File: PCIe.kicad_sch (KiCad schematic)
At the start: 24 parts, among them J12 10018783-11200TLF, U15 AP64501SP-13

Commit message: removed many unused parts
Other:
- company: © 2020-2022 Raspberry Pi Ltd (formerly Raspberry Pi (Trading) Ltd.) -> (none)
- title: Compute Module 4 IO Board - PCIe -> bitcart - PCIe
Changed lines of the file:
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@@
   (paper "A4")
   (title_block
-    (title "Compute Module 4 IO Board - PCIe")
+    (title "bitcart - PCIe")
+    (date "2022-06-02")
     (rev "1")
-    (company "© 2020-2022 Raspberry Pi Ltd (formerly Raspberry Pi (Trading) Ltd.)")
-    (comment 1 "www.raspberrypi.com")
+    (comment 1 "https://github.com/skot/bitcart.git")
   )
   (junction (at 157.734 152.654) (diameter 1.016) (color 0 0 0 0)

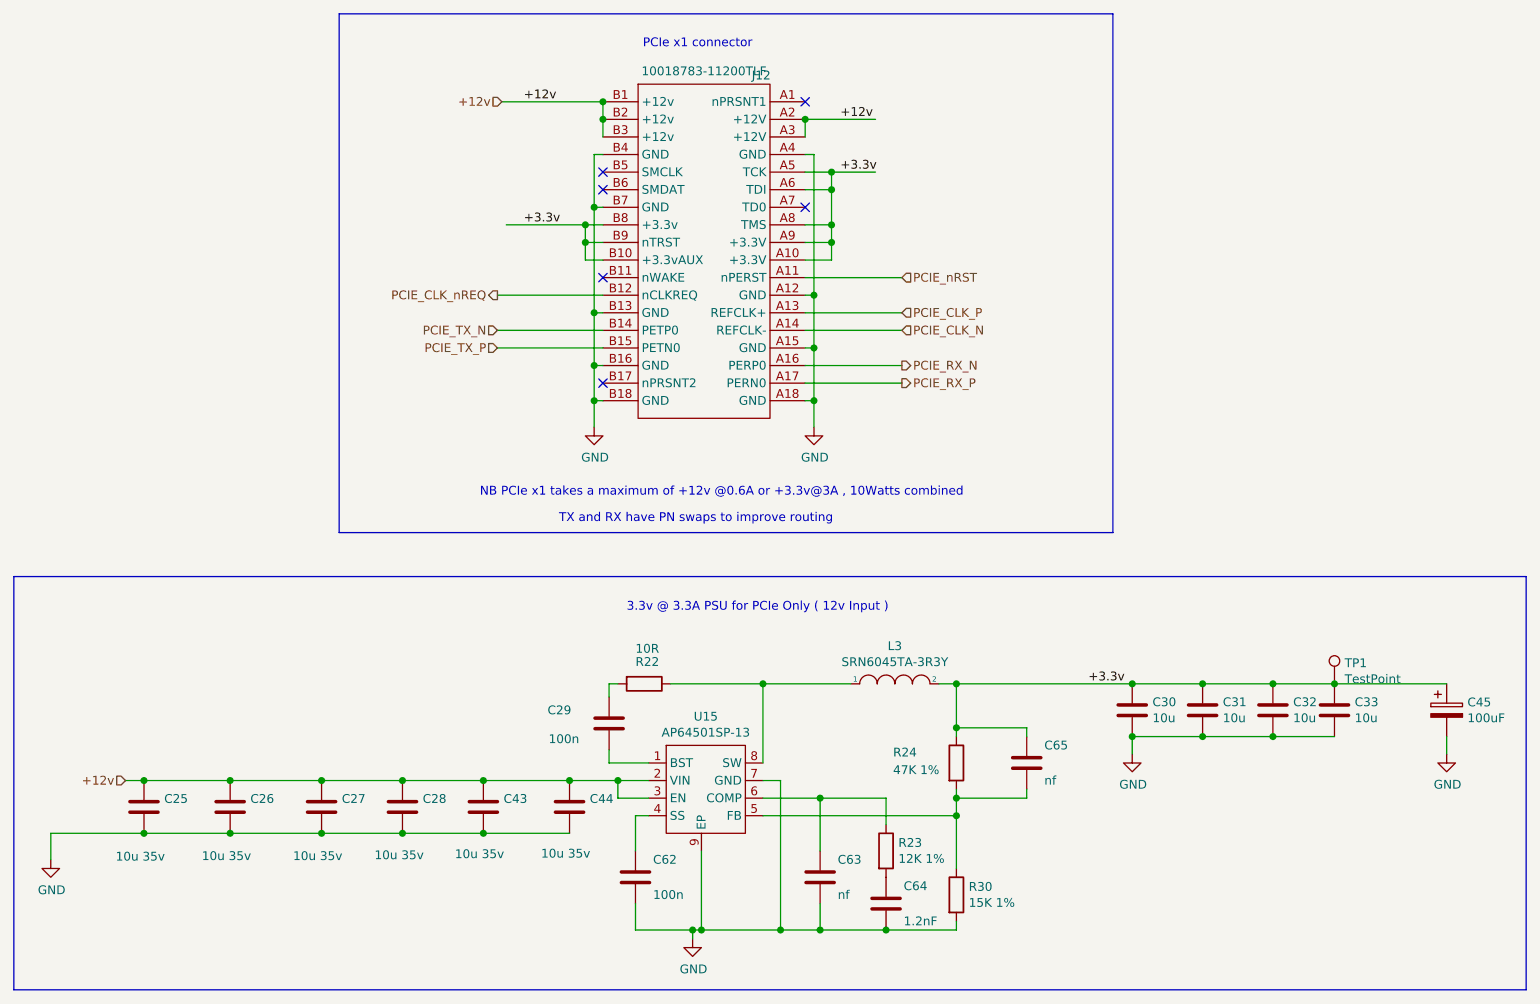
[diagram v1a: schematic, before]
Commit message: added M.2 m-key connector to schematic
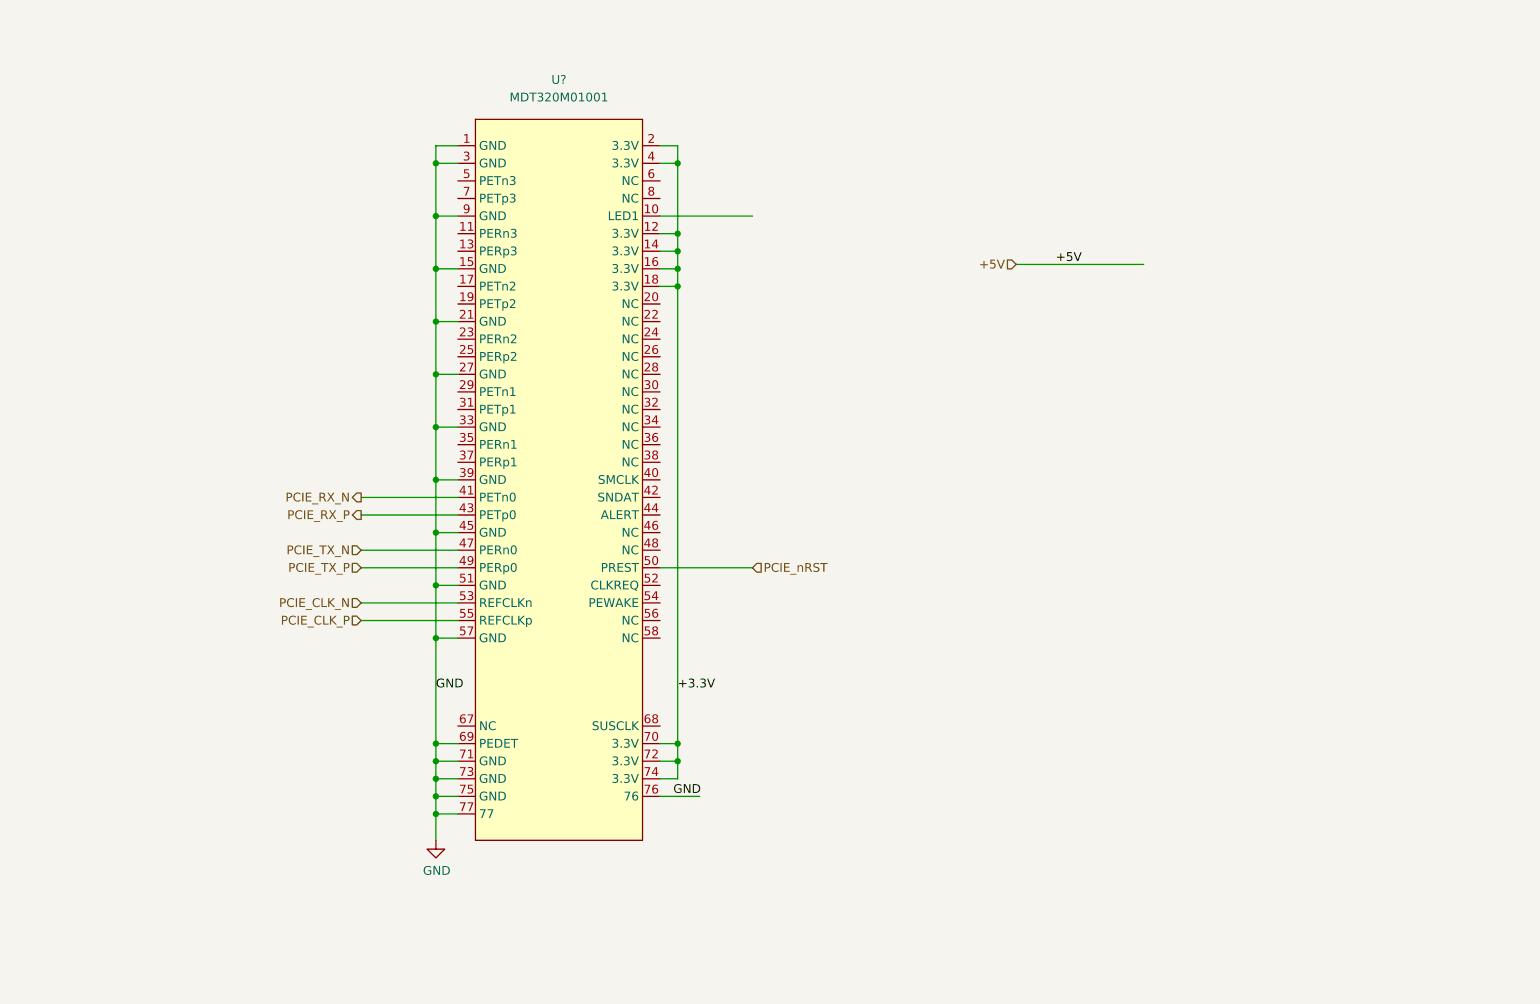
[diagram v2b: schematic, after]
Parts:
- removed C25, C26, C27, C28, C43, C44: 10u 35v, Capacitor_SMD:C_0805_2012Metric, symbol Device:C
- removed C29, C62: 100n, Capacitor_SMD:C_0402_1005Metric, symbol Device:C
- removed C30, C31, C32, C33: 10u, Capacitor_SMD:C_0805_2012Metric, symbol Device:C
- removed C45: 100uF, Capacitor_Tantalum_SMD:CP_EIA-7343-31_Kemet-D, symbol Device:CP
- removed C63, C65: nf, Capacitor_SMD:C_0402_1005Metric, symbol Device:C
- removed C64: 1.2nF, Capacitor_SMD:C_0402_1005Metric, symbol Device:C
- removed J12: 10018783-11200TLF, CM4IO:PCIex1-36, symbol CM4IO:PCIe-x1
- removed L3: SRN6045TA-3R3Y, Inductor_SMD:L_Bourns_SRN6045TA, symbol pspice:INDUCTOR
- removed R22: 10R, Resistor_SMD:R_0402_1005Metric, symbol Device:R
- removed R23: 12K 1%, Resistor_SMD:R_0402_1005Metric, symbol Device:R
- removed R24: 47K 1%, Resistor_SMD:R_0402_1005Metric, symbol Device:R
- removed R30: 15K 1%, Resistor_SMD:R_0402_1005Metric, symbol Device:R
- removed TP1: TestPoint, TestPoint:TestPoint_Pad_2.0x2.0mm, symbol Connector:TestPoint
- removed U15: AP64501SP-13, Package_SO:SOIC-8-1EP_3.9x4.9mm_P1.27mm_EP2.95x4.9mm_Mask2.71x3.4mm_ThermalVias, symbol CM4IO:AP64351
- added U?: MDT320M01001, symbol bitcart:MDT320M01001
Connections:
- net GND: now also U?.1 (GND), U?.15 (GND), U?.21 (GND), U?.27 (GND), U?.3 (GND), U?.33 (GND), U?.39 (GND), U?.45 (GND), U?.51 (GND), U?.57 (GND), U?.69 (PEDET), U?.71 (GND), U?.73 (GND), U?.75 (GND), U?.76, U?.77, U?.9 (GND)
- net PCIE_CLK_N: now also U?.53 (REFCLKn)
- net PCIE_CLK_P: now also U?.55 (REFCLKp)
- net PCIE_RX_N: now also U?.41 (PETn0)
- net PCIE_RX_P: now also U?.43 (PETp0)
- net PCIE_TX_N: now also U?.47 (PERn0)
- net PCIE_TX_P: now also U?.49 (PERp0)
- net PCIE_nRST: now also U?.50 (PREST)
- new net +3.3V: U?.12 (3.3V), U?.14 (3.3V), U?.16 (3.3V), U?.18 (3.3V), U?.2 (3.3V), U?.4 (3.3V), U?.70 (3.3V), U?.72 (3.3V), U?.74 (3.3V)
- no-connect marks 6 -> 0
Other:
- note removed: "3.3v @ 3.3A PSU for PCIe Only ( 12v Input )"
- note removed: "NB PCIe x1 takes a maximum of +12v @0.6A or +3.3v@3A , 10Watts combined"
- note removed: "PCIe x1 connector"
- note removed: "TX and RX have PN swaps to improve routing"

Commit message: removed unused components
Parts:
- U12: renamed from U?; DK (none) -> MDT320M01001CT-ND; PARTNO (none) -> MDT320M01001
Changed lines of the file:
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@@
   (symbol (lib_id "bitcart:MDT320M01001") (at 126.365 82.55 0) (unit 1)
     (in_bom yes) (on_board yes) (fields_autoplaced)
-    (property "Reference" "U?" (id 0) (at 125.73 29.845 0))
+    (property "Reference" "U12" (id 0) (at 125.73 29.845 0))
     (property "Value" "MDT320M01001" (id 1) (at 125.73 32.385 0))
     (property "Footprint" "" (id 2) (at 117.475 33.02 0)
@@
       (effects (font (size 1.27 1.27)) hide)
     )
+    (property "PARTNO" "MDT320M01001" (id 4) (at 126.365 82.55 0)
+      (effects (font (size 1.27 1.27)) hide)
+    )
+    (property "DK" "MDT320M01001CT-ND" (id 5) (at 126.365 82.55 0)
+      (effects (font (size 1.27 1.27)) hide)
+    )

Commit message: added the M.2 connector and MP8008 footprints
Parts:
- added H2: M2.5 x 2.5mm SMD threaded standoff, bitcart:9774025151R, symbol Mechanical:MountingHole
- U12: footprint (none) -> bitcart:MDT320M01001; DK MDT320M01001CT-ND -> MDT420M01001CT-ND; Drawing (none) -> https://cdn.amphenol-cs.com/media/wysiwyg/files/drawing/mdt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; PARTNO MDT320M01001 -> MDT420M01001
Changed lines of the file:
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@@
     (pin "1")
+  )
+  (symbol (lib_id "Mechanical:MountingHole") (at 125.73 155.575 0) (unit 1)
+    (in_bom yes) (on_board yes) (fields_autoplaced)
+    (property "Reference" "H2" (id 0) (at 128.27 154.3049 0)
+      (effects (font (size 1.27 1.27)) (justify left))
+    )
+    (property "Value" "M2.5 x 2.5mm SMD threaded standoff " (id 1) (at 128.27 156.8449 0)
+      (effects (font (size 1.27 1.27)) (justify left))
+    )
+    (property "Footprint" "bitcart:9774025151R" (id 2) (at 125.73 155.575 0)
+      (effects (font (size 1.27 1.27)) hide)
+    )
+    (property "Datasheet" "https://media.digikey.com/pdf/Data%20Sheets/Wurth%20Electronics%20PDFs/WA-SMSx_Performance_Flyer.pdf" (id 3) (at 125.73 155.575 0)
+      (effects (font (size 1.27 1.27)) hide)
+    )
+    (property "DK" "732-7078-1-ND" (id 4) (at 125.73 155.575 0)
+      (effects (font (size 1.27 1.27)) hide)
+    )
+    (property "PARTNO" "9774025151R" (id 5) (at 125.73 155.575 0)
+      (effects (font (size 1.27 1.27)) hide)
+    )
   )
   (symbol (lib_id "bitcart:MDT320M01001") (at 126.365 82.55 0) (unit 1)
@@
     (property "Reference" "U12" (id 0) (at 125.73 29.845 0))
     (property "Value" "MDT320M01001" (id 1) (at 125.73 32.385 0))
-    (property "Footprint" "" (id 2) (at 117.475 33.02 0)
+    (property "Footprint" "bitcart:MDT320M01001" (id 2) (at 117.475 33.02 0)
       (effects (font (size 1.27 1.27)) hide)
     )
-    (property "Datasheet" "" (id 3) (at 117.475 33.02 0)
+    (property "Datasheet" "https://www.amphenol-cs.com/media/wysiwyg/files/documentation/datasheet/ssio/ssio_pcie_m2.pdf" (id 3) (at 117.475 33.02 0)
       (effects (font (size 1.27 1.27)) hide)
     )
-    (property "PARTNO" "MDT320M01001" (id 4) (at 126.365 82.55 0)
+    (property "PARTNO" "MDT420M01001" (id 4) (at 126.365 82.55 0)
       (effects (font (size 1.27 1.27)) hide)
     )
-    (property "DK" "MDT320M01001CT-ND" (id 5) (at 126.365 82.55 0)
+    (property "DK" "MDT420M01001CT-ND" (id 5) (at 126.365 82.55 0)
       (effects (font (size 1.27 1.27)) hide)
     )
+    (property "Drawing" "https://cdn.amphenol-cs.com/media/wysiwyg/files/drawing/mdtxxxxxx001.pdf" (id 6) (at 126.365 82.55 0)
+      (effects (font (size 1.27 1.27)) hide)
+    )
